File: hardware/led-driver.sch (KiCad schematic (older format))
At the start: 9 parts, among them Q1 BC547

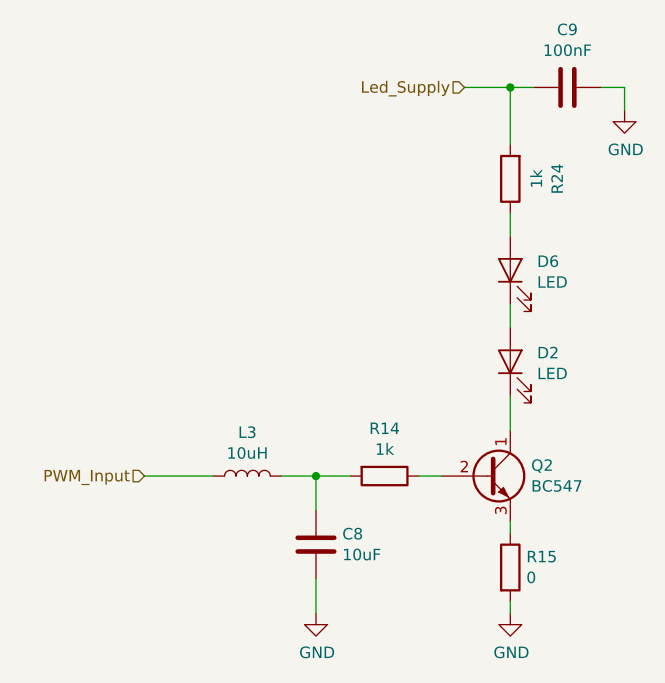
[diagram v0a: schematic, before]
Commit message: Assign footprints; add led supply circuit
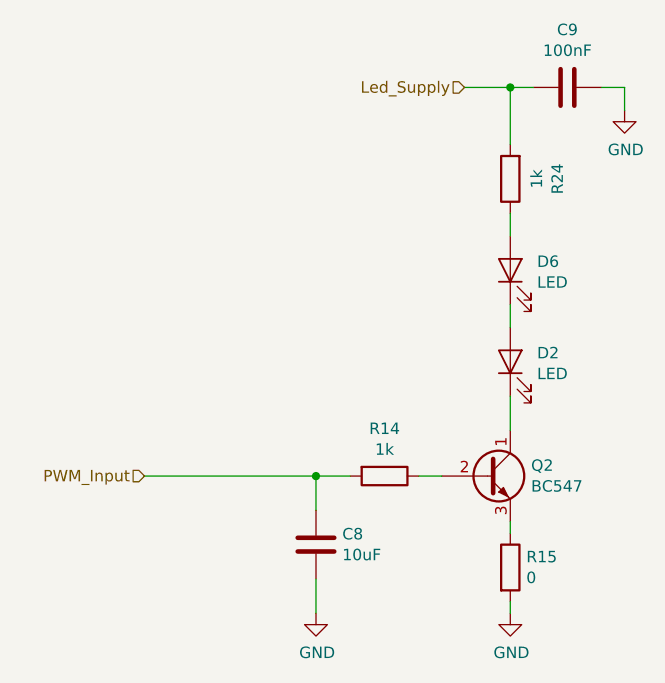
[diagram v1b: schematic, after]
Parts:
- removed L4: 10uH, symbol Device:L
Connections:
- net PWM_Input: now also C5.2, R12.2
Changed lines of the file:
@@
 $Descr A4 11693 8268
 encoding utf-8
-Sheet 2 4
+Sheet 3 4
 Title ""
 Date ""
@@
 	-1   0    0    1
 $EndComp
-$Comp
-L Device:L L4
-U 1 1 5C8ECEF6
-P 3100 3100
-AR Path="/5C8EC687/5C8ECEF6" Ref="L4"  Part="1"
-AR Path="/5C8EFAFF/5C8ECEF6" Ref="L3"  Part="1"
-F 0 "L3" V 3290 3100 50  0000 C CNN
-F 1 "10uH" V 3199 3100 50  0000 C CNN
-F 2 "" H 3100 3100 50  0001 C CNN
-F 3 "~" H 3100 3100 50  0001 C CNN
-	1    3100 3100
-	0    -1   -1   0
-$EndComp
-Wire Wire Line
-	3250 3100 3400 3100
 Wire Wire Line
 	3400 3250 3400 3100
@@
 Wire Wire Line
 	3400 3550 3400 3700
-Wire Wire Line
-	2650 3100 2950 3100
 $Comp
 L Device:LED D5
@@
 Wire Wire Line
 	4250 2350 4250 2450
+Wire Wire Line
+	2650 3100 3400 3100
 $EndSCHEMATC

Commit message: Fix footprints
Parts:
- C5, C7: footprint Capacitors_SMD:C_0805 -> Capacitor_SMD:C_0805_2012Metric_Pad1.15x1.40mm_HandSolder
- R12, R13, R23: footprint Resistors_SMD:R_0805 -> Resistor_SMD:R_0805_2012Metric_Pad1.15x1.40mm_HandSolder
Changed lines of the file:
@@
 F 0 "R15" H 4320 3546 50  0000 L CNN
 F 1 "0" H 4320 3455 50  0000 L CNN
-F 2 "Resistors_SMD:R_0805" V 4180 3500 50  0001 C CNN
+F 2 "Resistor_SMD:R_0805_2012Metric_Pad1.15x1.40mm_HandSolder" V 4180 3500 50  0001 C CNN
 F 3 "" H 4250 3500 50  0001 C CNN
 	1    4250 3500
@@
 F 0 "R14" V 3493 3100 50  0000 C CNN
 F 1 "1k" V 3584 3100 50  0000 C CNN
-F 2 "Resistors_SMD:R_0805" V 3630 3100 50  0001 C CNN
+F 2 "Resistor_SMD:R_0805_2012Metric_Pad1.15x1.40mm_HandSolder" V 3630 3100 50  0001 C CNN
 F 3 "" H 3700 3100 50  0001 C CNN
 	1    3700 3100
@@
 F 0 "C9" V 4248 1400 50  0000 C CNN
 F 1 "100nF" V 4339 1400 50  0000 C CNN
-F 2 "Capacitors_SMD:C_0805" H 4538 1250 50  0001 C CNN
+F 2 "Capacitor_SMD:C_0805_2012Metric_Pad1.15x1.40mm_HandSolder" H 4538 1250 50  0001 C CNN
 F 3 "" H 4500 1400 50  0001 C CNN
 	1    4500 1400
@@
 F 0 "C8" H 3285 3354 50  0000 R CNN
 F 1 "10uF" H 3285 3445 50  0000 R CNN
-F 2 "Capacitors_SMD:C_0805" H 3438 3250 50  0001 C CNN
+F 2 "Capacitor_SMD:C_0805_2012Metric_Pad1.15x1.40mm_HandSolder" H 3438 3250 50  0001 C CNN
 F 3 "" H 3400 3400 50  0001 C CNN
 	1    3400 3400
@@
 F 0 "R24" V 4043 1800 50  0000 C CNN
 F 1 "1k" V 4134 1800 50  0000 C CNN
-F 2 "Resistors_SMD:R_0805" V 4180 1800 50  0001 C CNN
+F 2 "Resistor_SMD:R_0805_2012Metric_Pad1.15x1.40mm_HandSolder" V 4180 1800 50  0001 C CNN
 F 3 "" H 4250 1800 50  0001 C CNN
 	1    4250 1800

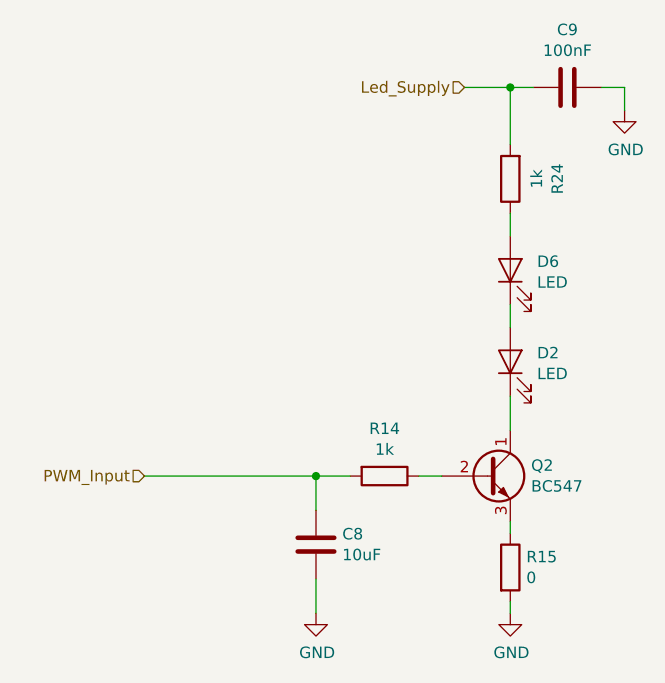
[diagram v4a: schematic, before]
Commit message: Add missing manufacturer links
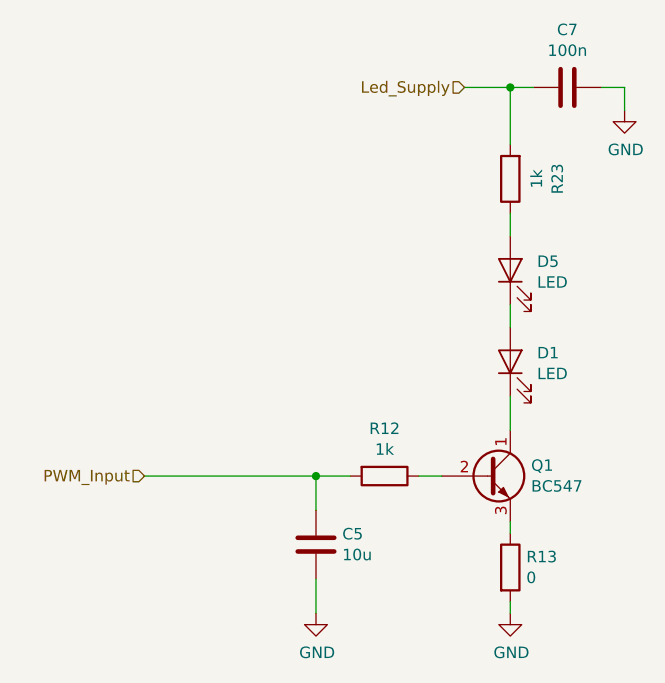
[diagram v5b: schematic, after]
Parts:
- C5: value 10uF -> 10u; Supplier (none) -> RS; Supplier Link (none) -> https://de.rs-online.com/web/p/keramik-vielschichtkondensat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; Supplier Part Number (none) -> 144-9030
- C7: value 100nF -> 100n; Supplier (none) -> RS; Supplier Link (none) -> https://de.rs-online.com/web/p/keramik-vielschichtkondensat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; Supplier Part Number (none) -> 170-0041
- Q1: Supplier (none) -> RS; Supplier Link (none) -> https://de.rs-online.com/web/p/bipolare-transistoren/166298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; Supplier Part Number (none) -> 166-2988
- R12, R23: Supplier (none) -> RS; Supplier Link (none) -> https://de.rs-online.com/web/p/smd-widerstande/8046449/; Supplier Part Number (none) -> 804-6449
- R13: Supplier (none) -> RS; Supplier Link (none) -> https://de.rs-online.com/web/p/smd-widerstande/6790800/; Supplier Part Number (none) -> 679-0800
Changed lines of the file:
@@
 EESchema Schematic File Version 4
-LIBS:uMIDI-wah-cache
-EELAYER 29 0
+EELAYER 30 0
 EELAYER END
 $Descr A4 11693 8268
 encoding utf-8
-Sheet 3 5
+Sheet 2 5
 Title ""
 Date ""
@@
 AR Path="/5C8EC687/5C8EC7F4" Ref="Q1"  Part="1"
 AR Path="/5C8EFAFF/5C8EC7F4" Ref="Q2"  Part="1"
-F 0 "Q2" H 4341 3146 50  0000 L CNN
+F 0 "Q1" H 4341 3146 50  0000 L CNN
 F 1 "BC547" H 4341 3055 50  0000 L CNN
 F 2 "Package_TO_SOT_THT:TO-92_Inline" H 4350 3025 50  0001 L CIN
 F 3 "http://www.fairchildsemi.com/ds/BC/BC547.pdf" H 4150 3100 50  0001 L CNN
+F 4 "RS" H 4341 3146 50  0001 L CNN "Supplier"
+F 5 "166-2988" H 4341 3146 50  0001 L CNN "Supplier Part Number"
+F 6 "https://de.rs-online.com/web/p/bipolare-transistoren/1662988/" H 4341 3146 50  0001 L CNN "Supplier Link"
 	1    4150 3100
 	1    0    0    -1
@@
 AR Path="/5C8EC687/5C8EC98B" Ref="D1"  Part="1"
 AR Path="/5C8EFAFF/5C8EC98B" Ref="D2"  Part="1"
-F 0 "D2" V 4288 2483 50  0000 R CNN
+F 0 "D1" V 4288 2483 50  0000 R CNN
 F 1 "LED" V 4197 2483 50  0000 R CNN
 F 2 "LED_SMD:LED_0805_2012Metric" H 4250 2600 50  0001 C CNN
@@
 AR Path="/5C8EC687/5C8ECB18" Ref="R13"  Part="1"
 AR Path="/5C8EFAFF/5C8ECB18" Ref="R15"  Part="1"
-F 0 "R15" H 4320 3546 50  0000 L CNN
+F 0 "R13" H 4320 3546 50  0000 L CNN
 F 1 "0" H 4320 3455 50  0000 L CNN
 F 2 "Resistor_SMD:R_0805_2012Metric_Pad1.15x1.40mm_HandSolder" V 4180 3500 50  0001 C CNN
 F 3 "" H 4250 3500 50  0001 C CNN
+F 4 "RS" H 4320 3546 50  0001 L CNN "Supplier"
+F 5 "679-0800" H 4320 3546 50  0001 L CNN "Supplier Part Number"
+F 6 "https://de.rs-online.com/web/p/smd-widerstande/6790800/" H 4320 3546 50  0001 L CNN "Supplier Link"
 	1    4250 3500
 	1    0    0    -1
@@
 AR Path="/5C8EC687/5C8ECBDB" Ref="R12"  Part="1"
 AR Path="/5C8EFAFF/5C8ECBDB" Ref="R14"  Part="1"
-F 0 "R14" V 3493 3100 50  0000 C CNN
+F 0 "R12" V 3493 3100 50  0000 C CNN
 F 1 "1k" V 3584 3100 50  0000 C CNN
 F 2 "Resistor_SMD:R_0805_2012Metric_Pad1.15x1.40mm_HandSolder" V 3630 3100 50  0001 C CNN
 F 3 "" H 3700 3100 50  0001 C CNN
+F 4 "RS" V 3493 3100 50  0001 C CNN "Supplier"
+F 5 "804-6449" V 3493 3100 50  0001 C CNN "Supplier Part Number"
+F 6 "https://de.rs-online.com/web/p/smd-widerstande/8046449/" V 3493 3100 50  0001 C CNN "Supplier Link"
 	1    3700 3100
 	0    1    1    0
@@
 AR Path="/5C8EC687/5C8ECCDD" Ref="C7"  Part="1"
 AR Path="/5C8EFAFF/5C8ECCDD" Ref="C9"  Part="1"
-F 0 "C9" V 4248 1400 50  0000 C CNN
-F 1 "100nF" V 4339 1400 50  0000 C CNN
+F 0 "C7" V 4248 1400 50  0000 C CNN
+F 1 "100n" V 4339 1400 50  0000 C CNN
 F 2 "Capacitor_SMD:C_0805_2012Metric_Pad1.15x1.40mm_HandSolder" H 4538 1250 50  0001 C CNN
 F 3 "" H 4500 1400 50  0001 C CNN
+F 4 "RS" V 4248 1400 50  0001 C CNN "Supplier"
+F 5 "170-0041" V 4248 1400 50  0001 C CNN "Supplier Part Number"
+F 6 "https://de.rs-online.com/web/p/keramik-vielschichtkondensatoren/1700041/" V 4248 1400 50  0001 C CNN "Supplier Link"
+F 7 "" V 4248 1400 50  0001 C CNN "Manufacturer"
+F 8 "" V 4248 1400 50  0001 C CNN "Manufacturer Part Number"
 	1    4500 1400
 	0    1    1    0
@@
 AR Path="/5C8EC687/5C8ECE43" Ref="C5"  Part="1"
 AR Path="/5C8EFAFF/5C8ECE43" Ref="C8"  Part="1"
-F 0 "C8" H 3285 3354 50  0000 R CNN
-F 1 "10uF" H 3285 3445 50  0000 R CNN
+F 0 "C5" H 3285 3354 50  0000 R CNN
+F 1 "10u" H 3285 3445 50  0000 R CNN
 F 2 "Capacitor_SMD:C_0805_2012Metric_Pad1.15x1.40mm_HandSolder" H 3438 3250 50  0001 C CNN
 F 3 "" H 3400 3400 50  0001 C CNN
+F 4 "RS" H 3285 3354 50  0001 R CNN "Supplier"
+F 5 "144-9030" H 3285 3354 50  0001 R CNN "Supplier Part Number"
+F 6 "https://de.rs-online.com/web/p/keramik-vielschichtkondensatoren/1449030/" H 3285 3354 50  0001 R CNN "Supplier Link"
 	1    3400 3400
 	-1   0    0    1
@@
 AR Path="/5C8EC687/5CD989FA" Ref="D5"  Part="1"
 AR Path="/5C8EFAFF/5CD989FA" Ref="D6"  Part="1"
-F 0 "D6" V 4288 2083 50  0000 R CNN
+F 0 "D5" V 4288 2083 50  0000 R CNN
 F 1 "LED" V 4197 2083 50  0000 R CNN
 F 2 "LED_SMD:LED_0805_2012Metric" H 4250 2200 50  0001 C CNN
@@
 AR Path="/5C8EC687/5CD998D9" Ref="R23"  Part="1"
 AR Path="/5C8EFAFF/5CD998D9" Ref="R24"  Part="1"
-F 0 "R24" V 4043 1800 50  0000 C CNN
+F 0 "R23" V 4043 1800 50  0000 C CNN
 F 1 "1k" V 4134 1800 50  0000 C CNN
 F 2 "Resistor_SMD:R_0805_2012Metric_Pad1.15x1.40mm_HandSolder" V 4180 1800 50  0001 C CNN
 F 3 "" H 4250 1800 50  0001 C CNN
+F 4 "RS" V 4043 1800 50  0001 C CNN "Supplier"
+F 5 "804-6449" V 4043 1800 50  0001 C CNN "Supplier Part Number"
+F 6 "https://de.rs-online.com/web/p/smd-widerstande/8046449/" V 4043 1800 50  0001 C CNN "Supplier Link"
 	1    4250 1800
 	-1   0    0    1

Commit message: Revision BOM: Get low-tech parts from Reichelt
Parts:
- C5: Manufacturer (none) -> MURATA; Manufacturer Part Number (none) -> GRM21BR61C106KE15L; Supplier RS -> Reichelt; Supplier Link https://de.rs-online.com/web/p/keramik-vielschichtkondensat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 -> https://www.reichelt.de/smd-vielschichtkondensator-g0805-10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; Supplier Part Number 144-9030 -> X5R-G0805 10/16
- C7: Manufacturer (none) -> YAGEO; Manufacturer Part Number (none) -> CC0805KRX7R9BB104; Supplier RS -> Reichelt; Supplier Link https://de.rs-online.com/web/p/keramik-vielschichtkondensat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 -> https://www.reichelt.de/smd-vielschicht-keramikkondensator-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; Supplier Part Number 170-0041 -> X7R-G0805 100N
- D1, D5: Supplier Link https://de.rs-online.com/web/p/leds-sichtbares-licht/700789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 -> https://www.rsonline-privat.de/Products/ProductDetail/ROHM-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; Supplier Part Number 700-7890 -> 7007890
- Q1: Manufacturer (none) -> DIOTEC; Manufacturer Part Number (none) -> BC547B; Supplier RS -> Reichelt; Supplier Link https://de.rs-online.com/web/p/bipolare-transistoren/166298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 -> https://www.reichelt.de/bipolartransistor-npn-45v-0-1a-0-5w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; Supplier Part Number 166-2988 -> BC 547B DIO
- R12, R23: Manufacturer (none) -> YAGEO; Manufacturer Part Number (none) -> RC0805FR-071KL; Supplier RS -> Reichelt; Supplier Link https://de.rs-online.com/web/p/smd-widerstande/8046449/ -> https://www.reichelt.de/smd-widerstand-0805-1-0-kohm-125-mw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; Supplier Part Number 804-6449 -> SMD-0805 1,00K
- R13: Manufacturer (none) -> RND COMPONENTS; Manufacturer Part Number (none) -> RND 1550805S8F0000T5E; Supplier RS -> Reichelt; Supplier Link https://de.rs-online.com/web/p/smd-widerstande/6790800/ -> https://www.reichelt.de/smd-widerstand-0805-0-0-ohm-125-mw-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; Supplier Part Number 679-0800 -> RND 0805 1 0
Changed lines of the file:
@@
 F 2 "Package_TO_SOT_THT:TO-92_Inline" H 4350 3025 50  0001 L CIN
 F 3 "http://www.fairchildsemi.com/ds/BC/BC547.pdf" H 4150 3100 50  0001 L CNN
-F 4 "RS" H 4341 3146 50  0001 L CNN "Supplier"
-F 5 "166-2988" H 4341 3146 50  0001 L CNN "Supplier Part Number"
-F 6 "https://de.rs-online.com/web/p/bipolare-transistoren/1662988/" H 4341 3146 50  0001 L CNN "Supplier Link"
+F 4 "Reichelt" H 4341 3146 50  0001 L CNN "Supplier"
+F 5 "BC 547B DIO" H 4341 3146 50  0001 L CNN "Supplier Part Number"
+F 6 "https://www.reichelt.de/bipolartransistor-npn-45v-0-1a-0-5w-to-92-bc-547b-dio-p219082.html?&trstct=pos_1&nbc=1" H 4341 3146 50  0001 L CNN "Supplier Link"
+F 7 "DIOTEC" H 4341 3146 50  0001 L CNN "Manufacturer"
+F 8 "BC547B" H 4341 3146 50  0001 L CNN "Manufacturer Part Number"
 	1    4150 3100
 	1    0    0    -1
@@
 F 3 "http://datasheet.octopart.com/SML-210PTT86-Rohm-datasheet-12523978.pdf" H 4250 2600 50  0001 C CNN
 F 4 "RS" V 4288 2483 50  0001 R CNN "Supplier"
-F 5 "700-7890" V 4288 2483 50  0001 R CNN "Supplier Part Number"
-F 6 "https://de.rs-online.com/web/p/leds-sichtbares-licht/7007890/" V 4288 2483 50  0001 R CNN "Supplier Link"
+F 5 "7007890" V 4288 2483 50  0001 R CNN "Supplier Part Number"
+F 6 "https://www.rsonline-privat.de/Products/ProductDetail/ROHM-SML-21-SMD-LED-grun-2-2-V-rechteckige-Linse-2012-0805-7007890" V 4288 2483 50  0001 R CNN "Supplier Link"
 F 7 "ROHM" V 4288 2483 50  0001 R CNN "Manufacturer"
 F 8 "SML-210PTT86" V 4288 2483 50  0001 R CNN "Manufacturer Part Number"
@@
 F 1 "0" H 4320 3455 50  0000 L CNN
 F 2 "Resistor_SMD:R_0805_2012Metric_Pad1.15x1.40mm_HandSolder" V 4180 3500 50  0001 C CNN
-F 3 "" H 4250 3500 50  0001 C CNN
-F 4 "RS" H 4320 3546 50  0001 L CNN "Supplier"
-F 5 "679-0800" H 4320 3546 50  0001 L CNN "Supplier Part Number"
-F 6 "https://de.rs-online.com/web/p/smd-widerstande/6790800/" H 4320 3546 50  0001 L CNN "Supplier Link"
+F 3 "https://docs-emea.rs-online.com/webdocs/13f1/0900766b813f17c1.pdf" H 4250 3500 50  0001 C CNN
+F 4 "Reichelt" H 4320 3546 50  0001 L CNN "Supplier"
+F 5 "RND 0805 1 0" H 4320 3546 50  0001 L CNN "Supplier Part Number"
+F 6 "https://www.reichelt.de/smd-widerstand-0805-0-0-ohm-125-mw-rnd-0805-1-0-p212707.html?&nbc=1" H 4320 3546 50  0001 L CNN "Supplier Link"
+F 7 "RND COMPONENTS" H 4320 3546 50  0001 L CNN "Manufacturer"
+F 8 "RND 1550805S8F0000T5E" H 4320 3546 50  0001 L CNN "Manufacturer Part Number"
 	1    4250 3500
 	1    0    0    -1
@@
 F 1 "1k" V 3584 3100 50  0000 C CNN
 F 2 "Resistor_SMD:R_0805_2012Metric_Pad1.15x1.40mm_HandSolder" V 3630 3100 50  0001 C CNN
-F 3 "" H 3700 3100 50  0001 C CNN
-F 4 "RS" V 3493 3100 50  0001 C CNN "Supplier"
-F 5 "804-6449" V 3493 3100 50  0001 C CNN "Supplier Part Number"
-F 6 "https://de.rs-online.com/web/p/smd-widerstande/8046449/" V 3493 3100 50  0001 C CNN "Supplier Link"
+F 3 "https://docs-emea.rs-online.com/webdocs/13af/0900766b813aff0c.pdf" H 3700 3100 50  0001 C CNN
+F 4 "Reichelt" V 3493 3100 50  0001 C CNN "Supplier"
+F 5 "SMD-0805 1,00K" V 3493 3100 50  0001 C CNN "Supplier Part Number"
+F 6 "https://www.reichelt.de/smd-widerstand-0805-1-0-kohm-125-mw-1-smd-0805-1-00k-p32886.html?&trstct=pol_0&nbc=1" V 3493 3100 50  0001 C CNN "Supplier Link"
+F 7 "YAGEO" V 3493 3100 50  0001 C CNN "Manufacturer"
+F 8 "RC0805FR-071KL" V 3493 3100 50  0001 C CNN "Manufacturer Part Number"
 	1    3700 3100
 	0    1    1    0
@@
 F 1 "100n" V 4339 1400 50  0000 C CNN
 F 2 "Capacitor_SMD:C_0805_2012Metric_Pad1.15x1.40mm_HandSolder" H 4538 1250 50  0001 C CNN
-F 3 "" H 4500 1400 50  0001 C CNN
-F 4 "RS" V 4248 1400 50  0001 C CNN "Supplier"
-F 5 "170-0041" V 4248 1400 50  0001 C CNN "Supplier Part Number"
-F 6 "https://de.rs-online.com/web/p/keramik-vielschichtkondensatoren/1700041/" V 4248 1400 50  0001 C CNN "Supplier Link"
-F 7 "" V 4248 1400 50  0001 C CNN "Manufacturer"
-F 8 "" V 4248 1400 50  0001 C CNN "Manufacturer Part Number"
+F 3 "https://docs-emea.rs-online.com/webdocs/0eb3/0900766b80eb3145.pdf" H 4500 1400 50  0001 C CNN
+F 4 "Reichelt" V 4248 1400 50  0001 C CNN "Supplier"
+F 5 "X7R-G0805 100N" V 4248 1400 50  0001 C CNN "Supplier Part Number"
+F 6 "https://www.reichelt.de/smd-vielschicht-keramikkondensator-100n-10-x7r-g0805-100n-p31879.html?&trstct=pol_1&nbc=1" V 4248 1400 50  0001 C CNN "Supplier Link"
+F 7 "YAGEO" V 4248 1400 50  0001 C CNN "Manufacturer"
+F 8 "CC0805KRX7R9BB104" V 4248 1400 50  0001 C CNN "Manufacturer Part Number"
 	1    4500 1400
 	0    1    1    0
@@
 F 1 "10u" H 3285 3445 50  0000 R CNN
 F 2 "Capacitor_SMD:C_0805_2012Metric_Pad1.15x1.40mm_HandSolder" H 3438 3250 50  0001 C CNN
-F 3 "" H 3400 3400 50  0001 C CNN
-F 4 "RS" H 3285 3354 50  0001 R CNN "Supplier"
-F 5 "144-9030" H 3285 3354 50  0001 R CNN "Supplier Part Number"
-F 6 "https://de.rs-online.com/web/p/keramik-vielschichtkondensatoren/1449030/" H 3285 3354 50  0001 R CNN "Supplier Link"
+F 3 "https://docs-emea.rs-online.com/webdocs/15fb/0900766b815fb3af.pdf" H 3400 3400 50  0001 C CNN
+F 4 "Reichelt" H 3285 3354 50  0001 R CNN "Supplier"
+F 5 "X5R-G0805 10/16" H 3285 3354 50  0001 R CNN "Supplier Part Number"
+F 6 "https://www.reichelt.de/smd-vielschichtkondensator-g0805-10-f-16v-x5r-g0805-10-16-p89734.html?&trstct=pol_0&nbc=1" H 3285 3354 50  0001 R CNN "Supplier Link"
+F 7 "MURATA" H 3285 3354 50  0001 R CNN "Manufacturer"
+F 8 "GRM21BR61C106KE15L" H 3285 3354 50  0001 R CNN "Manufacturer Part Number"
 	1    3400 3400
 	-1   0    0    1
@@
 F 3 "http://datasheet.octopart.com/SML-210PTT86-Rohm-datasheet-12523978.pdf" H 4250 2200 50  0001 C CNN
 F 4 "RS" V 4288 2083 50  0001 R CNN "Supplier"
-F 5 "700-7890" V 4288 2083 50  0001 R CNN "Supplier Part Number"
-F 6 "https://de.rs-online.com/web/p/leds-sichtbares-licht/7007890/" V 4288 2083 50  0001 R CNN "Supplier Link"
+F 5 "7007890" V 4288 2083 50  0001 R CNN "Supplier Part Number"
+F 6 "https://www.rsonline-privat.de/Products/ProductDetail/ROHM-SML-21-SMD-LED-grun-2-2-V-rechteckige-Linse-2012-0805-7007890" V 4288 2083 50  0001 R CNN "Supplier Link"
 F 7 "ROHM" V 4288 2083 50  0001 R CNN "Manufacturer"
 F 8 "SML-210PTT86" V 4288 2083 50  0001 R CNN "Manufacturer Part Number"
@@
 F 1 "1k" V 4134 1800 50  0000 C CNN
 F 2 "Resistor_SMD:R_0805_2012Metric_Pad1.15x1.40mm_HandSolder" V 4180 1800 50  0001 C CNN
-F 3 "" H 4250 1800 50  0001 C CNN
-F 4 "RS" V 4043 1800 50  0001 C CNN "Supplier"
-F 5 "804-6449" V 4043 1800 50  0001 C CNN "Supplier Part Number"
-F 6 "https://de.rs-online.com/web/p/smd-widerstande/8046449/" V 4043 1800 50  0001 C CNN "Supplier Link"
+F 3 "https://docs-emea.rs-online.com/webdocs/13af/0900766b813aff0c.pdf" H 4250 1800 50  0001 C CNN
+F 4 "Reichelt" V 4043 1800 50  0001 C CNN "Supplier"
+F 5 "SMD-0805 1,00K" V 4043 1800 50  0001 C CNN "Supplier Part Number"
+F 6 "https://www.reichelt.de/smd-widerstand-0805-1-0-kohm-125-mw-1-smd-0805-1-00k-p32886.html?&trstct=pol_0&nbc=1" V 4043 1800 50  0001 C CNN "Supplier Link"
+F 7 "YAGEO" V 4043 1800 50  0001 C CNN "Manufacturer"
+F 8 "RC0805FR-071KL" V 4043 1800 50  0001 C CNN "Manufacturer Part Number"
 	1    4250 1800
 	-1   0    0    1
